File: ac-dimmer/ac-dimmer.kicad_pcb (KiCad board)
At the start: 2 copper layers, 74 parts, among them J1 Screw_Terminal_01x02, J2 Screw_Terminal_01x02, J3 Screw_Terminal_01x02, J4 Screw_Terminal_01x02, J5 Conn_01x06_Pin, J6 Screw_Terminal_01x02, Q1 IRF840, Q10 IRF840, Q11 KSP44, Q12 KSP44, Q2 IRF840, Q3 IRF840, Q4 IRF840, Q5 KSP44, Q6 KSP44, Q7 IRF840, Q8 IRF840, Q9 IRF840, U1 FL5150MX, U2 FL5150MX, U3 FL5150MX, U4 FL5150MX, U5 MCP4451

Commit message: Finish AC dimmer layout and add production files
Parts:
- removed C10, C9: 22nF, Capacitor_SMD:C_1206_3216Metric
- removed C11, C12, C6: 4.7uF, Capacitor_SMD:C_1206_3216Metric
- removed C13, C14, C15, C16, C17, C7, C8: 0.1uF, Capacitor_SMD:C_1206_3216Metric
- removed D2, D3, D4: 1N4007, Diode_THT:D_DO-41_SOD81_P10.16mm_Horizontal
- removed J4: Screw_Terminal_01x02, TerminalBlock_Phoenix:TerminalBlock_Phoenix_MKDS-1,5-2-5.08_1x02_P5.08mm_Horizontal
- removed J5: Conn_01x06_Pin, Connector_PinHeader_2.54mm:PinHeader_1x06_P2.54mm_Vertical
- removed JP2, JP3, JP4: Jumper_3_Open, Connector_PinHeader_2.54mm:PinHeader_1x03_P2.54mm_Vertical
- removed JP5, JP6: SolderJumper_3_Open, Jumper:SolderJumper-3_P1.3mm_Open_Pad1.0x1.5mm
- removed Q10, Q2, Q4, Q7, Q8, Q9: IRF840, Package_TO_SOT_THT:TO-220-3_Vertical
- removed Q11, Q12, Q6: KSP44, Package_TO_SOT_THT:TO-92_Inline
- removed R14, R15, R16, R19, R20: 2MR, Resistor_SMD:R_1206_3216Metric
- removed R17, R18: 1kR, Resistor_SMD:R_1206_3216Metric
- removed R21, R22: 330kR, Resistor_SMD:R_1206_3216Metric
- removed R23, R24: 33kR, Resistor_SMD:R_1206_3216Metric
- removed U2, U3, U4: FL5150MX, Package_SO:SSOP-10_3.9x4.9mm_P1.00mm
- removed U5: MCP4451, Package_SO:TSSOP-20_4.4x6.5mm_P0.65mm
- added G***: LOGO, LOGO, F.Cu at (135.9, 45.7)
- added H1: MountingHole, MountingHole:MountingHole_2.7mm_M2.5_ISO7380, F.Cu at (115.0, 43.0)
- added H2: MountingHole, MountingHole:MountingHole_2.7mm_M2.5_ISO7380, F.Cu at (161.0, 43.0)
- added H3: MountingHole, MountingHole:MountingHole_2.7mm_M2.5_ISO7380, F.Cu at (161.0, 75.0)
- added H4: MountingHole, MountingHole:MountingHole_2.7mm_M2.5_ISO7380, F.Cu at (115.0, 75.0)
- C3, C4: value 22nF -> 10nF
- J3: value Screw_Terminal_01x02 -> Conn_01x02_Pin; footprint TerminalBlock_Phoenix:TerminalBlock_Phoenix_MKDS-1,5-2-5.08_1x02_P5.08mm_Horizontal -> Connector_PinHeader_2.54mm:PinHeader_1x02_P2.54mm_Vertical
- R1, R2, R3, R4, R7: value 2MR -> 1MR
- R10: value 330kR -> 10k
- R11: value 33kR -> 10k
- R12: value 33kR -> 100k
- R13: value 2MR -> 100k
- R6: value 1kR -> 1MR
- R8: value 2MR -> 10k
- R9: value 330kR -> 100k
- moved J3 369.4 mm to (119.2, 55.9), turned to 0 degrees
- moved J1 348.4 mm to (152.8, 71.8)
- moved Q3 348.4 mm to (142.7, 71.8)
- moved J6 346.8 mm to (152.8, 51.4)
- moved Q5 343.8 mm to (119.8, 68.6), turned to -90 degrees
- moved J2 341.0 mm to (152.8, 61.6)
- moved R11 334.8 mm to (136.1, 71.8), turned to 0 degrees
- moved Q1 332.6 mm to (142.7, 51.4)
- moved R1 329.4 mm to (119.4, 50.2)
- moved C3 327.8 mm to (143.3, 57.0), turned to -90 degrees
- moved D1 325.5 mm to (135.1, 61.6)
- moved R7 317.8 mm to (130.0, 50.2)
- moved R5 317.1 mm to (130.2, 45.7)
- moved R9 316.7 mm to (136.2, 67.9)
- moved U1 314.4 mm to (128.7, 56.2)
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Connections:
- net /D_CAT_DIM_1 renamed /MAINS_NEUTRAL_CAT
- net /MODE_DIM_1 renamed /DIM_MODE
- net /VS_DIM_1 renamed /VS_DIM
- net VDD_DIM_1 renamed VDD
- C1 pad 2: GND_DIM_1 -> GND
- C2 pad 1: VDD_DIM_2 -> DIM_CTRL
- C2 pad 2: GND_DIM_2 -> GND
- C3 pad 1: /GATE_DIM_1 -> /GATE
- C3 pad 2: GND_DIM_1 -> GND
- C4 pad 1: Net-(Q2-G) -> /GATE
- C4 pad 2: GND_DIM_2 -> GND
- C5 pad 2: GND_DIM_1 -> GND
- J1 pad 1: MAINS_LIVE_OUT_1 -> MAINS_LIVE_OUT
- J2 pad 1: MAINS_LIVE_OUT_2 -> MAINS_LIVE_IN
- J3 pad 1: MAINS_LIVE_OUT_3 -> DIM_CTRL
- J3 pad 2: MAINS_NEUTRAL -> GND
- JP1 pad 3: GND_DIM_1 -> GND
- Q1 pad 1: /GATE_DIM_1 -> /GATE
- Q1 pad 3: GND_DIM_1 -> GND
- Q3 pad 1: /GATE_DIM_1 -> /GATE
- Q3 pad 2: MAINS_LIVE_OUT_1 -> MAINS_LIVE_OUT
- Q3 pad 3: GND_DIM_1 -> GND
- R1 pad 2: MAINS_LIVE_IN -> Net-(R1-Pad2)
- R10 pad 1: Net-(Q6-B) -> Net-(Q5-C)
- R10 pad 2: Net-(D2-K) -> Net-(R10-Pad2)
- R11 pad 1: Net-(Q5-C) -> Net-(R11-Pad1)
- R12 pad 1: Net-(Q6-C) -> Net-(R12-Pad1)
- R12 pad 2: Net-(D2-K) -> Net-(R12-Pad2)
- R13 pad 1: Net-(U3-OC_Sense1) -> /LP_DIM_1
- R13 pad 2: MAINS_LIVE_IN -> Net-(R12-Pad1)
- R2 pad 1: Net-(U2-OC_Sense1) -> Net-(R1-Pad2)
- R3 pad 1: MAINS_NEUTRAL -> Net-(R3-Pad1)
- R4 pad 1: MAINS_NEUTRAL -> Net-(R4-Pad1)
- R4 pad 2: Net-(U2-ZC_Monitor) -> MAINS_LIVE_OUT
- R5 pad 2: /GATE_DIM_1 -> /GATE
- R6 pad 1: Net-(U2-DRV_Gate) -> MAINS_NEUTRAL
- R6 pad 2: Net-(Q2-G) -> Net-(R3-Pad1)
- R7 pad 2: MAINS_LIVE_OUT_1 -> Net-(R4-Pad1)
- R8 pad 1: Net-(U2-OC_Sense2) -> Net-(R10-Pad2)
- R8 pad 2: MAINS_LIVE_OUT_2 -> Net-(R11-Pad1)
- R9 pad 1: /LP_DIM_1 -> Net-(R12-Pad2)
- U1 pad 2: DIM_CTRL_1 -> DIM_CTRL
- U1 pad 5: GND_DIM_1 -> GND
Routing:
- net GND: track 0.00 -> 72.1 mm
- net /VS_DIM: track 0.00 -> 62.7 mm
- net MAINS_NEUTRAL: track 0.00 -> 57.1 mm, vias 0 -> 1
- net /GATE: track 0.00 -> 42.1 mm
- net MAINS_LIVE_IN: track 0.00 -> 41.7 mm, vias 0 -> 1
- net MAINS_LIVE_OUT: track 0.00 -> 34.4 mm, vias 0 -> 1
- net VDD: track 0.00 -> 22.8 mm, vias 0 -> 2
- net /LP_DIM_1: track 0.00 -> 19.5 mm
- net Net-(U1-ZC_Monitor): track 0.00 -> 16.4 mm
- net Net-(U1-DRV_Gate): track 0.00 -> 15.1 mm
- net Net-(U1-OC_Sense1): track 0.00 -> 15.0 mm
- net /MAINS_NEUTRAL_CAT: track 0.00 -> 11.3 mm
- net Net-(U1-OC_Sense2): track 0.00 -> 9.40 mm, vias 0 -> 2
- net DIM_CTRL: track 0.00 -> 7.25 mm
- net /DIM_MODE: track 0.00 -> 5.74 mm
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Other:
- board outline added: 50 x 36 mm
- board text added: "AC Leading & Trailing Edge Dimmer v0.1 | github.com/niliha"
- board text added: "LEAD | TRAIL"
- board text added: "L_IN"
- board text added: "L_OUT"
- board text added: "N"
- board text added: "R_DIM 0-500k"

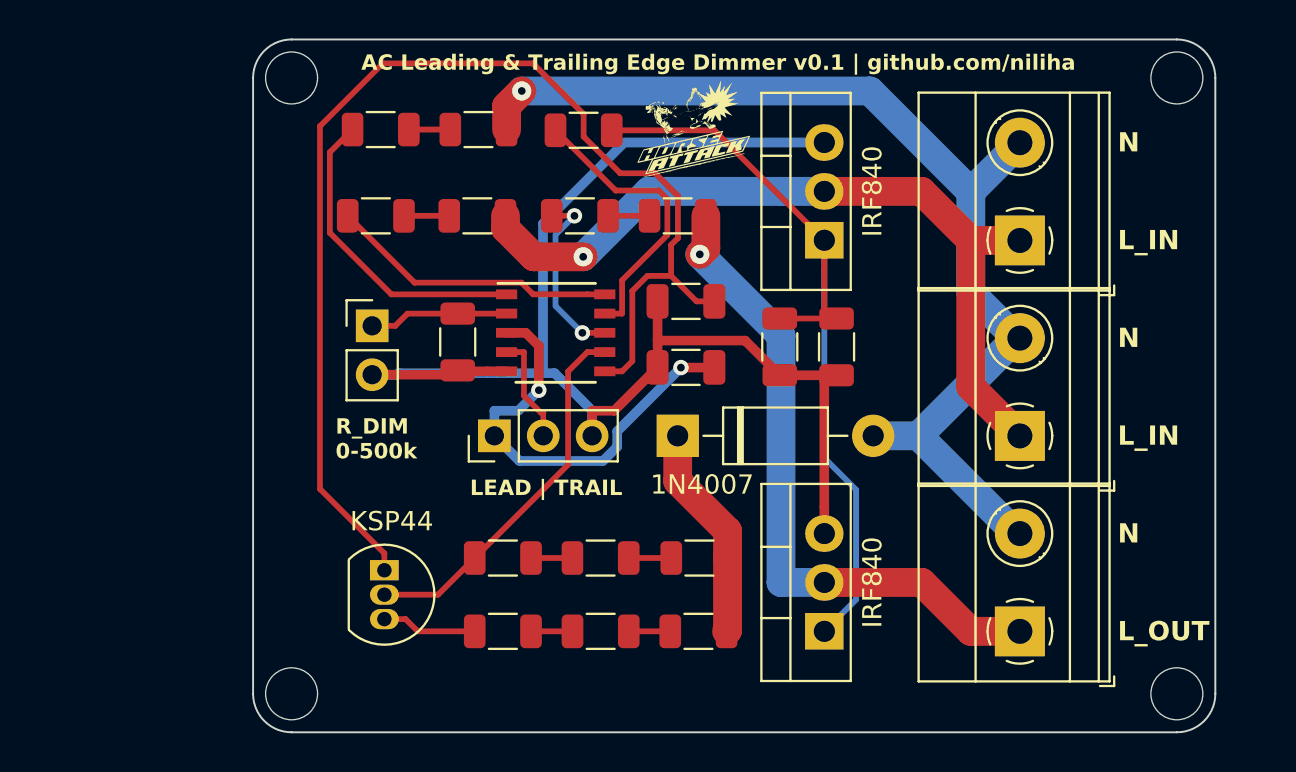
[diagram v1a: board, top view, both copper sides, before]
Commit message: Route 230V traces
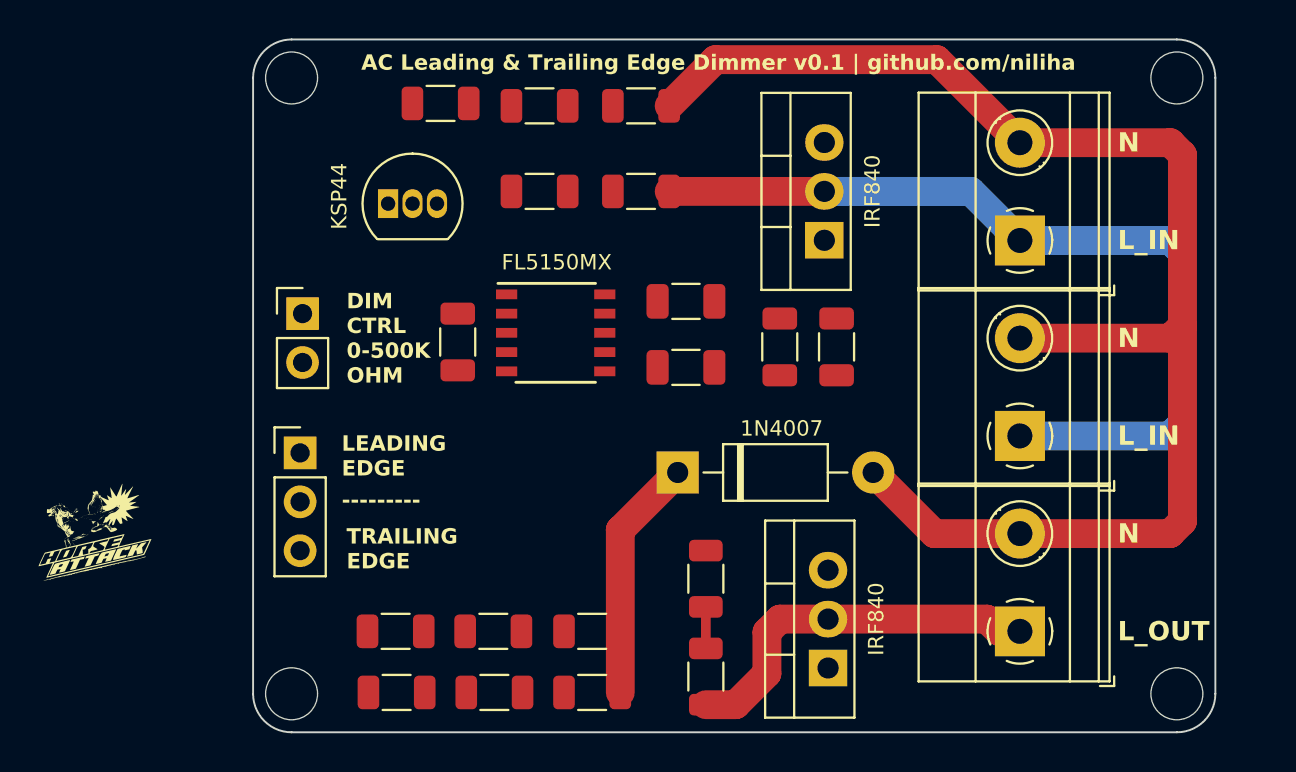
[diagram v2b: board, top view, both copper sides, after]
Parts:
- moved G*** 37.5 mm to (104.8, 66.7)
- moved R4 24.0 mm to (136.5, 74.1), turned to -90 degrees
- moved R7 20.0 mm to (136.5, 69.0), turned to -90 degrees
- moved Q5 19.1 mm to (120.0, 49.5), turned to 0 degrees
- moved JP1 10.1 mm to (115.4, 62.5), turned to 0 degrees
- moved R1 8.60 mm to (127.9, 48.9)
- moved R2 8.60 mm to (133.2, 48.9)
- moved R6 8.54 mm to (133.2, 44.5)
- moved R3 8.35 mm to (127.9, 44.5), turned to 0 degrees
- moved R5 7.57 mm to (122.7, 44.3)
- moved R12 6.75 mm to (125.5, 71.8)
- moved R13 6.75 mm to (120.4, 71.8)
- moved R9 6.75 mm to (130.6, 71.8)
- moved R10 6.37 mm to (120.5, 74.9)
- moved R8 6.37 mm to (125.5, 74.9)
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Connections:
- R3 pad 1: Net-(R3-Pad1) -> Net-(U1-ZC_Monitor)
- R3 pad 2: Net-(U1-ZC_Monitor) -> Net-(R3-Pad2)
- R6 pad 2: Net-(R3-Pad1) -> Net-(R3-Pad2)
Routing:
- net GND: track 72.1 -> 0.00 mm
- net /VS_DIM: track 62.7 -> 0.00 mm
- net /GATE: track 42.1 -> 0.00 mm
- net VDD: track 22.8 -> 0.00 mm, vias 2 -> 0
- net /LP_DIM_1: track 19.5 -> 0.00 mm
- net MAINS_NEUTRAL: track 57.1 -> 75.1 mm, vias 1 -> 0
- net Net-(U1-ZC_Monitor): track 16.4 -> 0.00 mm
- net Net-(U1-DRV_Gate): track 15.1 -> 0.00 mm
- net Net-(U1-OC_Sense1): track 15.0 -> 0.00 mm
- net MAINS_LIVE_OUT: track 34.4 -> 19.7 mm, vias 1 -> 0
- net Net-(U1-OC_Sense2): track 9.40 -> 0.00 mm, vias 2 -> 0
- net DIM_CTRL: track 7.25 -> 0.00 mm
- net /DIM_MODE: track 5.74 -> 0.00 mm
- net Net-(Q5-C): track 4.96 -> 0.00 mm
- net MAINS_LIVE_IN: track 41.7 -> 45.6 mm, vias 1 -> 0
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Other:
- board text added: "---------"
- board text added: "DIM CTRL 0-500K OHM"
- board text added: "LEADING EDGE"
- board text added: "TRAILING EDGE"
- board text removed: "LEAD | TRAIL"
- board text removed: "R_DIM 0-500k"

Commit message: Finish manual re-routing
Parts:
- moved R5 25.6 mm to (145.0, 57.0), turned to 90 degrees
- moved G*** 23.5 mm to (119.8, 48.5)
- moved Q5 18.5 mm to (127.5, 66.4)
- moved C1 8.64 mm to (127.0, 56.5), turned to -90 degrees
- moved R12 3.37 mm to (126.4, 75.0)
- moved R13 3.37 mm to (121.3, 75.0)
- moved R9 3.37 mm to (131.5, 75.0)
- moved U1 3.29 mm to (132.0, 56.0)
- moved R10 3.07 mm to (121.4, 72.0)
- moved R8 3.07 mm to (126.5, 72.0)
- moved R11 3.07 mm to (131.5, 72.0)
- moved C5 2.91 mm to (137.2, 57.0), turned to -90 degrees
- moved C3 0.88 mm to (142.4, 57.0)
- moved C4 0.57 mm to (139.8, 57.0)
- moved C2 0.30 mm to (123.5, 56.5)
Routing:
- net GND: track 0.00 -> 78.7 mm, vias 0 -> 1
- net /GATE: track 0.00 -> 44.9 mm
- net /VS_DIM: track 0.00 -> 32.0 mm
- net /LP_DIM_1: track 0.00 -> 31.2 mm, vias 0 -> 1
- net /DIM_MODE: track 0.00 -> 20.9 mm, vias 0 -> 1
- net VDD: track 0.00 -> 19.1 mm, vias 0 -> 1
- net Net-(U1-DRV_Gate): track 0.00 -> 17.3 mm, vias 0 -> 2
- net Net-(U1-OC_Sense2): track 0.00 -> 15.5 mm, vias 0 -> 2
- net DIM_CTRL: track 0.00 -> 15.4 mm
- net Net-(Q5-C): track 0.00 -> 13.9 mm
- net Net-(U1-ZC_Monitor): track 0.00 -> 12.8 mm
- net Net-(U1-OC_Sense1): track 0.00 -> 11.1 mm
- net Net-(R3-Pad2): track 0.00 -> 2.35 mm
- net Net-(R1-Pad2): track 0.00 -> 2.35 mm
- net Net-(R12-Pad2): track 0.00 -> 2.21 mm
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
